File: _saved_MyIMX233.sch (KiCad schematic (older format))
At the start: 72 parts, among them IC1 iMX233, IC2 DDR_SDRAM_MT46_x16, J1 USB_A, J2 Micro_SD_Card, P1 P4v2, P2 1v2, P3 VDDA1v8, P4 2v5, P5 3v3, SW1 SWITCH_PUSHBUTTON, Y1 24Mhz

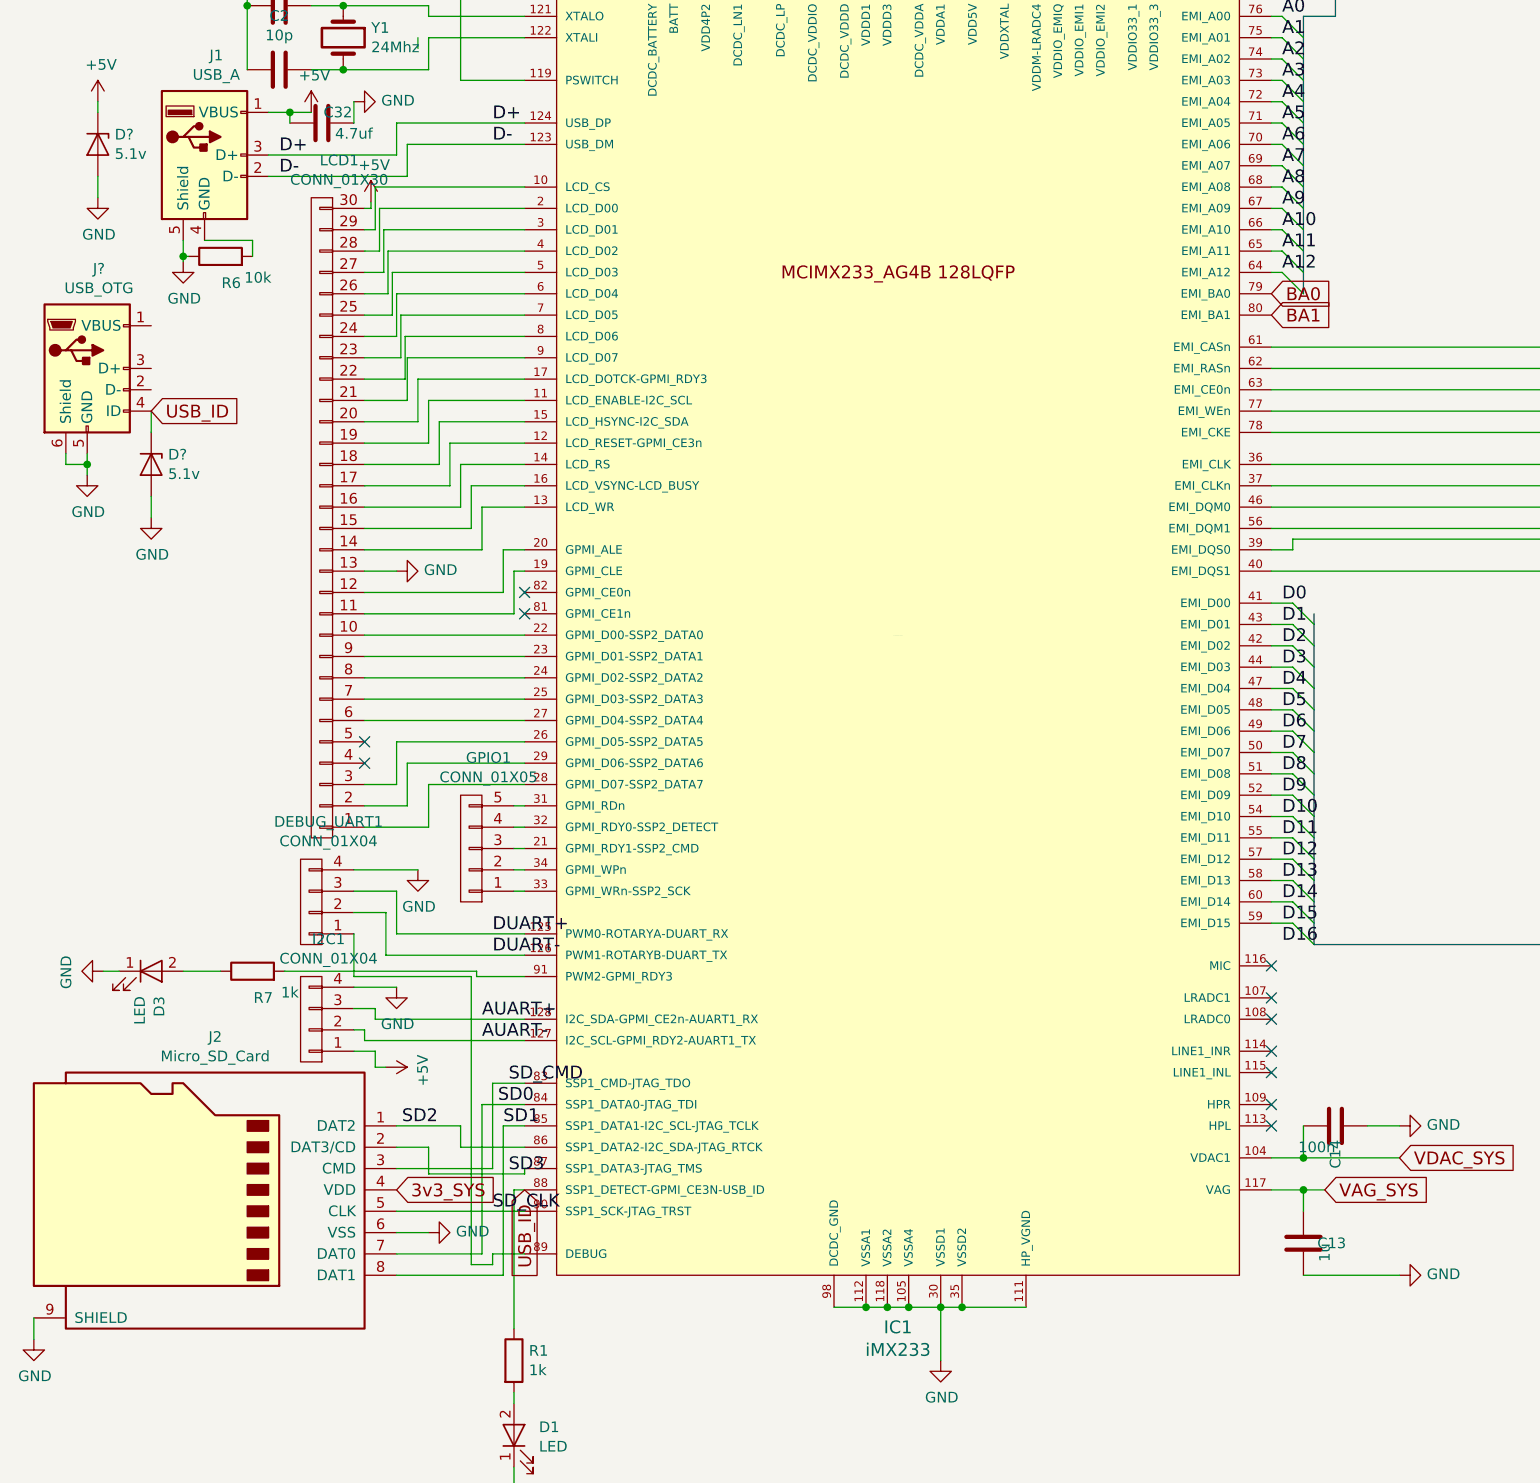
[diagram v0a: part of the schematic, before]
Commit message: updated README and added uSD mod and lib which might work without 3D
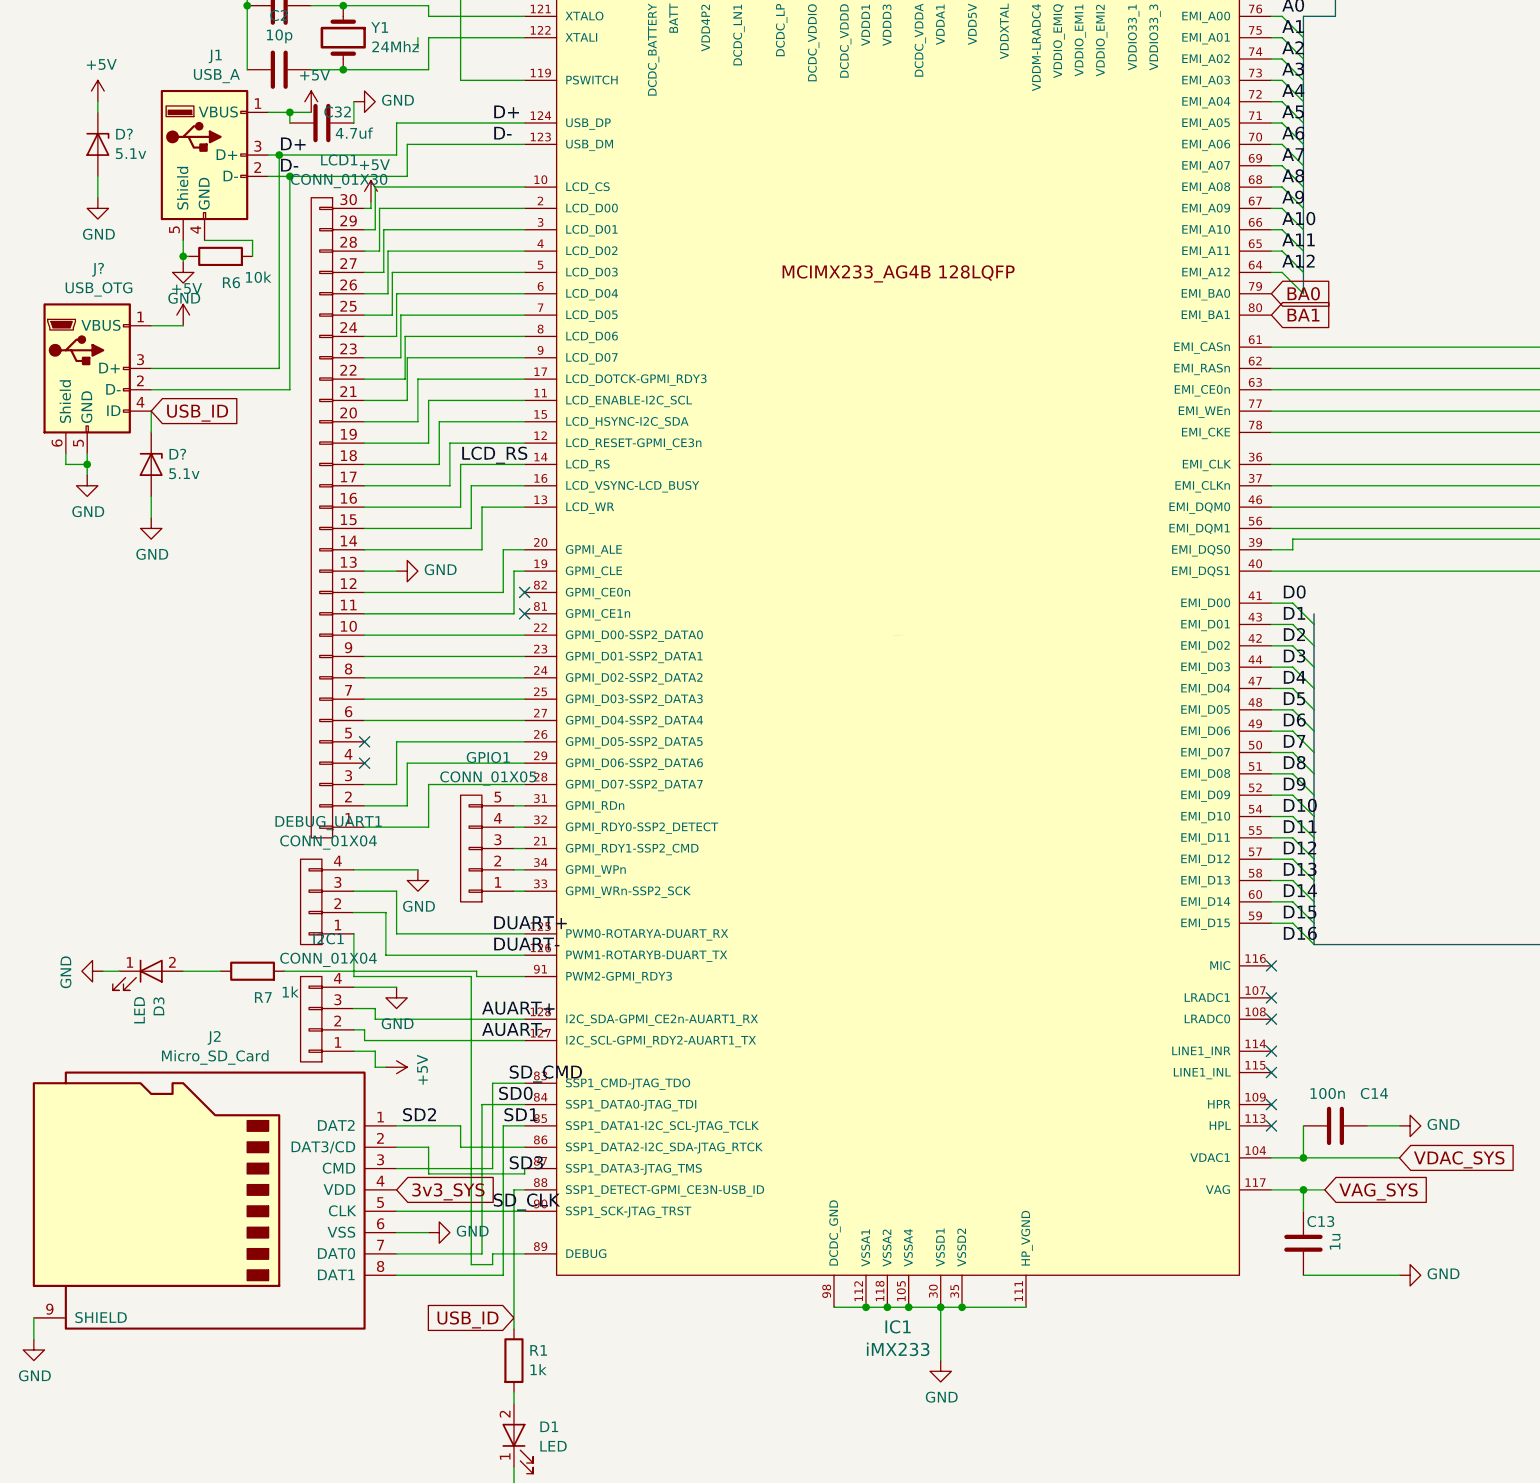
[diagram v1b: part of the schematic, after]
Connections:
- net D- is gone; now on net D+: IC1.123 (USB_DM), J1.2 (D-)
- net +5V: now also J?.1 (VBUS)
- net D+: now also J?.2 (D-), J?.3 (D+)
- net LCD_RS: now reaches IC1.14 (LCD_RS), LCD1.16 (P16)
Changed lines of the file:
@@
 U 1 1 590631C8
 P 6900 8750
-F 0 "C13" H 7100 8750 50  0000 R CNN
-F 1 "1u" V 7000 8750 50  0000 R CNN
+F 0 "C13" H 7050 8850 50  0000 R CNN
+F 1 "1u" V 7050 8800 50  0000 R CNN
 F 2 "Capacitors_SMD:C_0603_HandSoldering" H 6938 8600 50  0001 C CNN
 F 3 "" H 6900 8750 50  0001 C CNN
@@
 U 1 1 59063B35
 P 7050 8200
-F 0 "C14" H 7250 8200 50  0000 R CNN
-F 1 "100n" V 7150 8200 50  0000 R CNN
+F 0 "C14" V 6900 8450 50  0000 R CNN
+F 1 "100n" V 6900 8250 50  0000 R CNN
 F 2 "Capacitors_SMD:C_0402" H 7088 8050 50  0001 C CNN
 F 3 "" H 7050 8200 50  0001 C CNN
@@
 	1    0    0    -1
 $EndComp
-Text GLabel 3250 8500 3    60   Input ~ 0
+Text GLabel 3200 9100 0    60   Input ~ 0
 USB_ID
 Text GLabel 1500 4850 2    60   Input ~ 0
@@
 Wire Wire Line
 	2950 1950 2850 1950
+Text Label 2950 5100 0    60   ~ 0
+LCD_RS
+Wire Wire Line
+	1500 4650 2100 4650
+Wire Wire Line
+	2100 4650 2100 3650
+Connection ~ 2100 3650
+Wire Wire Line
+	2150 3750 2150 4750
+Wire Wire Line
+	2150 4750 1500 4750
+Connection ~ 2150 3750
+$Comp
+L +5V #PWR?
+U 1 1 5991413D
+P 1650 4450
+F 0 "#PWR?" H 1650 4300 50  0001 C CNN
+F 1 "+5V" H 1665 4623 50  0000 C CNN
+F 2 "" H 1650 4450 50  0001 C CNN
+F 3 "" H 1650 4450 50  0001 C CNN
+	1    1650 4450
+	1    0    0    -1
+$EndComp
+Wire Wire Line
+	1650 4450 1500 4450
 $EndSCHEMATC
